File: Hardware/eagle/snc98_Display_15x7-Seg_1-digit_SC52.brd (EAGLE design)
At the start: 154.9 x 33.5 mm, 62 parts, among them M10 IRLML2244, M11 IRLML2244, M4 IRLML2244, M5 IRLML2244, M6 IRLML2244, M7 IRLML2244, M8 IRLML2244, M9 IRLML2244, X1 MICROMATCH-12, X2 MICROMATCH-14, X3 MICROMATCH-12, X4 MICROMATCH-14

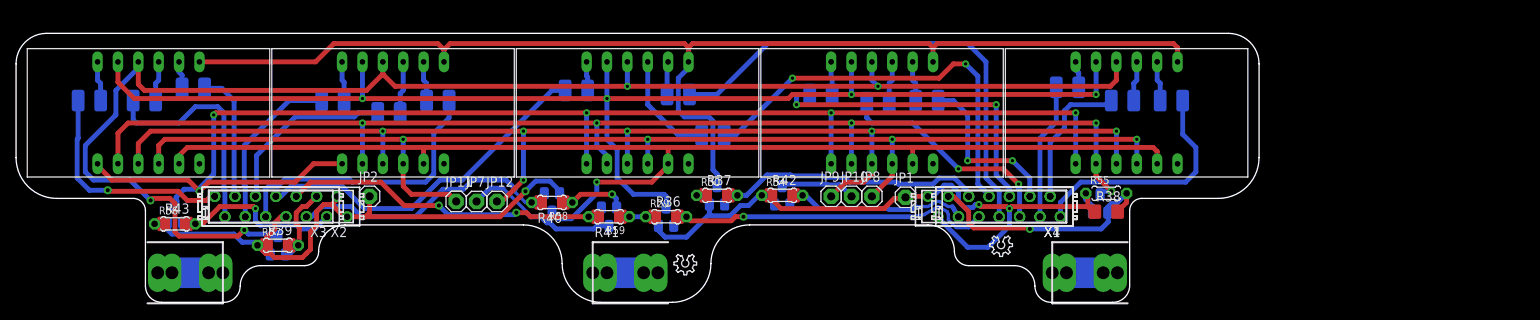
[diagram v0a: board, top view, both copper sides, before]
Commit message: Version 4 mechanical change
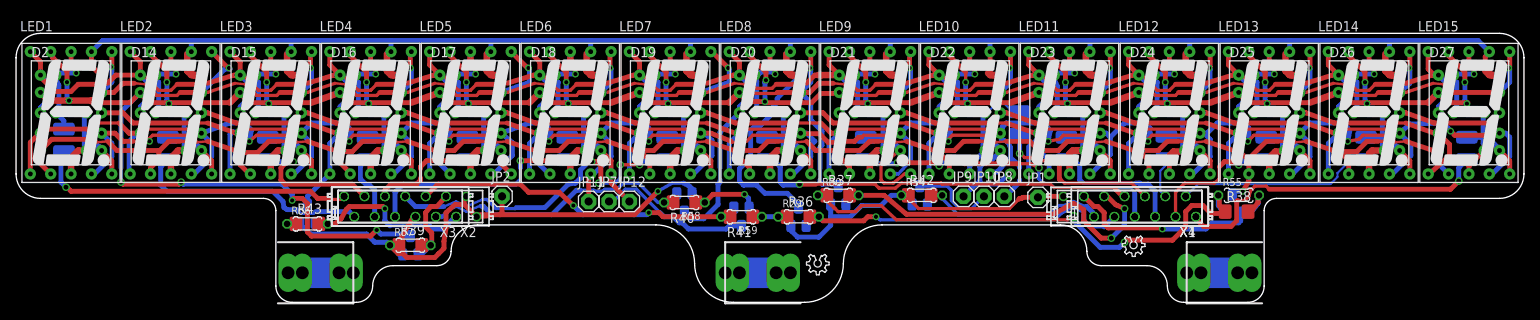
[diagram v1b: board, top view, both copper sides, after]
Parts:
- removed U$1, U$2, U$3, U$4, U$5: LTD040AUE-101A, display_LTD:LTD040AUE-101A
- added D14, D15, D16, D17, D18, D19, D2, D20, D21, D22, D23, D24, D25, D26, D27: SC40-11_UNISC40-11_UNI, display-hp:10MM_UNI
- added LED1, LED10, LED11, LED12, LED13, LED14, LED15, LED2, LED3, LED4, LED5, LED6, LED7, LED8, LED9: 7-SEG_SC52-11, display-kingbright:SA52-11
- moved R19 37.3 mm to (180.8, 19.2), turned to 270 degrees
- moved R18 30.9 mm to (168.3, 19.2), turned to 270 degrees
- moved R16 30.4 mm to (143.4, 19.3), turned to 270 degrees
- moved R17 25.9 mm to (155.8, 19.2), turned to 270 degrees
- moved R14 25.0 mm to (125.1, 22.4), turned to 270 degrees
- moved R13 24.3 mm to (105.9, 19.2), turned to 270 degrees
- moved R15 24.2 mm to (130.9, 19.2), turned to 270 degrees
- moved R54 17.4 mm to (112.9, 13.3)
- moved R10 17.2 mm to (68.7, 19.2), turned to 270 degrees
- moved M6 17.1 mm to (112.6, 13.3)
- moved R42 17.1 mm to (112.6, 13.3)
- moved X4 16.9 mm to (138.8, 11.9)
- moved X1 16.9 mm to (140.1, 11.9)
- moved BH4 16.8 mm to (150.2, 3.68)
- moved R55 16.5 mm to (152.4, 13.3)
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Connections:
- net DIG_0: now also D2.11, D2.12, D2.13, D2.14, LED1.3, LED1.8; no longer U$1.12
- net DIG_1: now also D14.11, D14.12, D14.13, D14.14, LED2.3, LED2.8; no longer U$1.9
- net DIG_10: now also D23.11, D23.12, D23.13, D23.14, LED11.3, LED11.8; no longer U$4.9
- net DIG_11: now also D24.11, D24.12, D24.13, D24.14, LED12.3, LED12.8; no longer U$4.8
- net DIG_12: now also D25.11, D25.12, D25.13, D25.14, LED13.3, LED13.8; no longer U$5.12
- net DIG_13: now also D26.11, D26.12, D26.13, D26.14, LED14.3, LED14.8; no longer U$5.9
- net DIG_14: now also D27.11, D27.12, D27.13, D27.14, LED15.3, LED15.8; no longer U$5.8
- net DIG_2: now also D15.11, D15.12, D15.13, D15.14, LED3.3, LED3.8; no longer U$1.8
- net DIG_3: now also D16.11, D16.12, D16.13, D16.14, LED4.3, LED4.8; no longer U$2.12
- net DIG_4: now also D17.11, D17.12, D17.13, D17.14, LED5.3, LED5.8; no longer U$2.9
- net DIG_5: now also D18.11, D18.12, D18.13, D18.14, LED6.3, LED6.8; no longer U$2.8
- net DIG_6: now also D19.11, D19.12, D19.13, D19.14, LED7.3, LED7.8; no longer U$3.12
- net DIG_7: now also D20.11, D20.12, D20.13, D20.14, LED8.3, LED8.8; no longer U$3.9
- net DIG_8: now also D21.11, D21.12, D21.13, D21.14, LED9.3, LED9.8; no longer U$3.8
- net DIG_9: now also D22.11, D22.12, D22.13, D22.14, LED10.3, LED10.8; no longer U$4.12
- net SEG_A: now also D14.10, D15.10, D16.10, D17.10, D18.10, D19.10, D2.10, D20.10, D21.10, D22.10, D23.10, D24.10, D25.10, D26.10, D27.10, LED1.7, LED10.7, LED11.7, LED12.7, LED13.7, LED14.7, LED15.7, LED2.7, LED3.7, LED4.7, LED5.7, LED6.7, LED7.7, LED8.7, LED9.7; no longer U$1.11, U$2.11, U$3.11, U$4.11, U$5.11
- net SEG_B: now also D14.9, D15.9, D16.9, D17.9, D18.9, D19.9, D2.9, D20.9, D21.9, D22.9, D23.9, D24.9, D25.9, D26.9, D27.9, LED1.6, LED10.6, LED11.6, LED12.6, LED13.6, LED14.6, LED15.6, LED2.6, LED3.6, LED4.6, LED5.6, LED6.6, LED7.6, LED8.6, LED9.6; no longer U$1.7, U$2.7, U$3.7, U$4.7, U$5.7
- net SEG_C: now also D14.7, D15.7, D16.7, D17.7, D18.7, D19.7, D2.7, D20.7, D21.7, D22.7, D23.7, D24.7, D25.7, D26.7, D27.7, LED1.4, LED10.4, LED11.4, LED12.4, LED13.4, LED14.4, LED15.4, LED2.4, LED3.4, LED4.4, LED5.4, LED6.4, LED7.4, LED8.4, LED9.4; no longer U$1.4, U$2.4, U$3.4, U$4.4, U$5.4
- net SEG_D: now also D14.5, D15.5, D16.5, D17.5, D18.5, D19.5, D2.5, D20.5, D21.5, D22.5, D23.5, D24.5, D25.5, D26.5, D27.5, LED1.2, LED10.2, LED11.2, LED12.2, LED13.2, LED14.2, LED15.2, LED2.2, LED3.2, LED4.2, LED5.2, LED6.2, LED7.2, LED8.2, LED9.2; no longer U$1.2, U$2.2, U$3.2, U$4.2, U$5.2
- net SEG_DP: now also D14.6, D14.8, D15.6, D15.8, D16.6, D16.8, D17.6, D17.8, D18.6, D18.8, D19.6, D19.8, D2.6, D2.8, D20.6, D20.8, D21.6, D21.8, D22.6, D22.8, D23.6, D23.8, D24.6, D24.8, D25.6, D25.8, D26.6, D26.8, D27.6, D27.8, LED1.5, LED10.5, LED11.5, LED12.5, LED13.5, LED14.5, LED15.5, LED2.5, LED3.5, LED4.5, LED5.5, LED6.5, LED7.5, LED8.5, LED9.5; no longer U$1.3, U$2.3, U$3.3, U$4.3, U$5.3
- net SEG_E: now also D14.4, D15.4, D16.4, D17.4, D18.4, D19.4, D2.4, D20.4, D21.4, D22.4, D23.4, D24.4, D25.4, D26.4, D27.4, LED1.1, LED10.1, LED11.1, LED12.1, LED13.1, LED14.1, LED15.1, LED2.1, LED3.1, LED4.1, LED5.1, LED6.1, LED7.1, LED8.1, LED9.1; no longer U$1.1, U$2.1, U$3.1, U$4.1, U$5.1
- net SEG_F: now also D14.2, D15.2, D16.2, D17.2, D18.2, D19.2, D2.2, D20.2, D21.2, D22.2, D23.2, D24.2, D25.2, D26.2, D27.2, LED1.9, LED10.9, LED11.9, LED12.9, LED13.9, LED14.9, LED15.9, LED2.9, LED3.9, LED4.9, LED5.9, LED6.9, LED7.9, LED8.9, LED9.9; no longer U$1.10, U$2.10, U$3.10, U$4.10, U$5.10
- net SEG_G: now also D14.1, D14.3, D15.1, D15.3, D16.1, D16.3, D17.1, D17.3, D18.1, D18.3, D19.1, D19.3, D2.1, D2.3, D20.1, D20.3, D21.1, D21.3, D22.1, D22.3, D23.1, D23.3, D24.1, D24.3, D25.1, D25.3, D26.1, D26.3, D27.1, D27.3, LED1.10, LED10.10, LED11.10, LED12.10, LED13.10, LED14.10, LED15.10, LED2.10, LED3.10, LED4.10, LED5.10, LED6.10, LED7.10, LED8.10, LED9.10; no longer U$1.5, U$2.5, U$3.5, U$4.5, U$5.5
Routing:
- net SEG_G: track 151.2 -> 358.5 mm, vias 1 -> 0
- net SEG_DP: track 159.4 -> 345.0 mm, vias 6 -> 0
- net SEG_F: track 183.9 -> 363.6 mm, vias 4 -> 34
- net SEG_C: track 152.0 -> 324.3 mm, vias 4 -> 12
- net SEG_A: track 161.9 -> 316.3 mm, vias 4 -> 0
- net SEG_B: track 151.4 -> 297.1 mm, vias 0 -> 15
- net SEG_E: track 174.8 -> 279.8 mm, vias 5 -> 0
- net SEG_D: track 152.9 -> 241.2 mm, vias 5 -> 1
- net DIG_9: track 4.12 -> 28.7 mm, vias 0 -> 1
- net CA_LED: track 188.6 -> 211.4 mm, vias 4 -> 3
- net DIG_6: track 3.61 -> 26.1 mm, vias 0 -> 1
- net DIG_2: track 3.46 -> 25.8 mm, vias 0 -> 1
- net DIG_8: track 4.12 -> 26.3 mm, vias 0 -> 1
- net DIG_10: track 5.24 -> 27.2 mm, vias 0 -> 1
- net DIG_12: track 4.38 -> 26.2 mm, vias 0 -> 1
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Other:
- board size 154.9 x 33.5 mm -> 188 x 33.5 mm

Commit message: PCB cleaning V1.1
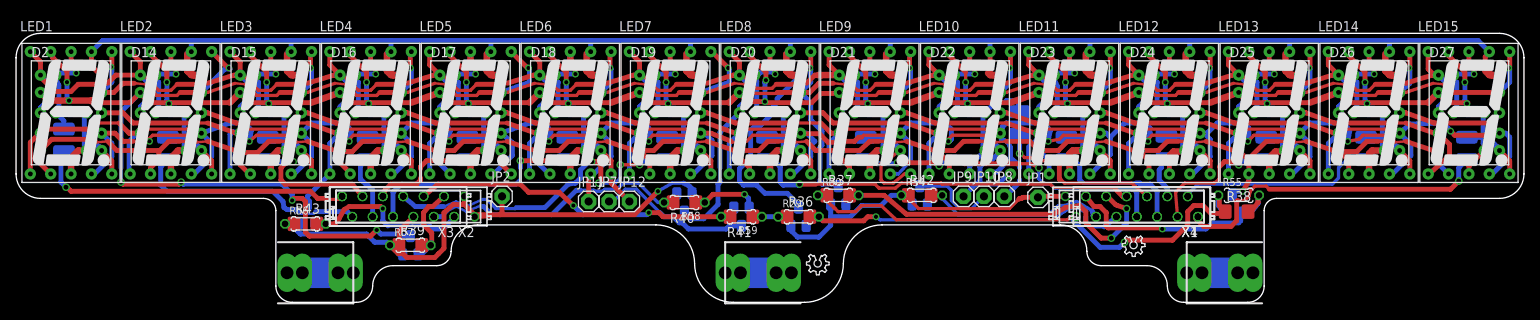
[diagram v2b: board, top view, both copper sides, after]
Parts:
- moved X1 0.25 mm to (140.3, 11.9)
- moved R43 0.25 mm to (36.1, 9.78)
- moved R56 0.25 mm to (36.1, 9.78)
- moved X2 0.25 mm to (48.9, 11.9)
- moved X3 0.25 mm to (47.6, 11.9)
- moved X4 0.25 mm to (139.1, 11.9)
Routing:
- net DIG_9: track 28.7 -> 29.6 mm
- net CA_LED: track 211.4 -> 212.1 mm
- net IO-E: track 23.2 -> 22.5 mm
- net DIG_7: track 27.0 -> 26.3 mm
- net D11_A: track 5.27 -> 5.78 mm

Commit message: PCB - add Tear Drop
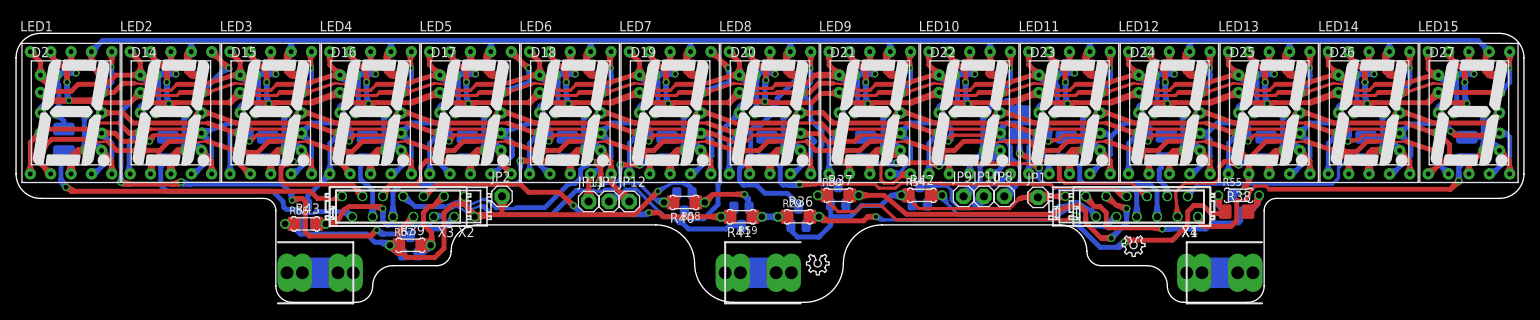
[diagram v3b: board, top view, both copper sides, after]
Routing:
- net SEG_F: track 363.7 -> 631.1 mm
- net SEG_DP: track 344.6 -> 562.2 mm
- net SEG_G: track 358.5 -> 567.2 mm
- net SEG_C: track 324.4 -> 524.2 mm
- net SEG_B: track 297.1 -> 487.1 mm
- net SEG_E: track 279.8 -> 435.1 mm
- net SEG_D: track 241.2 -> 383.4 mm
- net CA_LED: track 212.1 -> 328.6 mm
- net SEG_A: track 316.3 -> 411.4 mm
- net DIG_9: track 29.6 -> 60.5 mm
- net DIG_0: track 26.0 -> 56.7 mm
- net DIG_14: track 25.6 -> 54.1 mm
- net DIG_11: track 26.4 -> 54.7 mm
- net DIG_13: track 26.5 -> 54.7 mm
- net DIG_8: track 26.3 -> 54.5 mm
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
